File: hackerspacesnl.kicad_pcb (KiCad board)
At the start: 2 copper layers, 82.7 x 99.6 mm, 38 parts, among them J1 Screw_Terminal_01x02, J2 Conn_01x04_Male, Q1 Q_NMOS_GSD, Q2 Q_NMOS_GSD, Q3 Q_NMOS_GSD, Q4 Q_NMOS_GSD, Q5 Q_NMOS_GSD, Q6 Q_NMOS_GSD, SW1 SW_Push, SW2 SW_Push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

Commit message: led footprint
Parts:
- added D1: Red-GreenLED, hsnl:LED_0805_multicolor, F.Cu at (66.6, 90.7)
- added D10: Red-GreenLED, hsnl:LED_0805_multicolor, F.Cu at (80.0, 90.7)
- added D11: Red-GreenLED, hsnl:LED_0805_multicolor, F.Cu at (71.1, 99.9)
- added D12: Red-GreenLED, hsnl:LED_0805_multicolor, F.Cu at (75.5, 96.8)
- added D13: Red-GreenLED, hsnl:LED_0805_multicolor, F.Cu at (80.0, 93.8)
- added D14: Red-GreenLED, hsnl:LED_0805_multicolor, F.Cu at (84.4, 90.7)
- added D15: Red-GreenLED, hsnl:LED_0805_multicolor, F.Cu at (75.5, 99.9)
- added D2: Red-GreenLED, hsnl:LED_0805_multicolor, F.Cu at (66.6, 93.8)
- added D3: Red-GreenLED, hsnl:LED_0805_multicolor, F.Cu at (71.1, 90.7)
- added D4: Red-GreenLED, hsnl:LED_0805_multicolor, F.Cu at (66.6, 96.8)
- added D5: Red-GreenLED, hsnl:LED_0805_multicolor, F.Cu at (71.1, 93.8)
- added D6: Red-GreenLED, hsnl:LED_0805_multicolor, F.Cu at (75.5, 90.7)
- added D7: Red-GreenLED, hsnl:LED_0805_multicolor, F.Cu at (66.6, 99.9)
- added D8: Red-GreenLED, hsnl:LED_0805_multicolor, F.Cu at (71.1, 96.8)
- added D9: Red-GreenLED, hsnl:LED_0805_multicolor, F.Cu at (75.5, 93.8)

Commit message: board outline
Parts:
- moved D5 43.9 mm to (100.5, 126.4)
- moved D9 43.9 mm to (104.9, 126.4)
- moved D12 43.9 mm to (104.9, 129.5)
- moved D3 43.9 mm to (100.5, 123.4)
- moved D6 43.9 mm to (104.9, 123.4)
- moved D8 43.9 mm to (100.5, 129.5)
- moved D13 43.9 mm to (109.4, 126.4)
- moved D2 43.9 mm to (96.0, 126.4)
- moved D1 43.9 mm to (96.0, 123.4)
- moved D10 43.9 mm to (109.4, 123.4)
- moved D11 43.9 mm to (100.5, 132.5)
- moved D14 43.9 mm to (113.8, 123.4)
- moved D15 43.9 mm to (104.9, 132.5)
- moved D4 43.9 mm to (96.0, 129.5)
- moved D7 43.9 mm to (96.0, 132.5)
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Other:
- board size 82.7 x 99.6 mm -> 79.5 x 95.2 mm

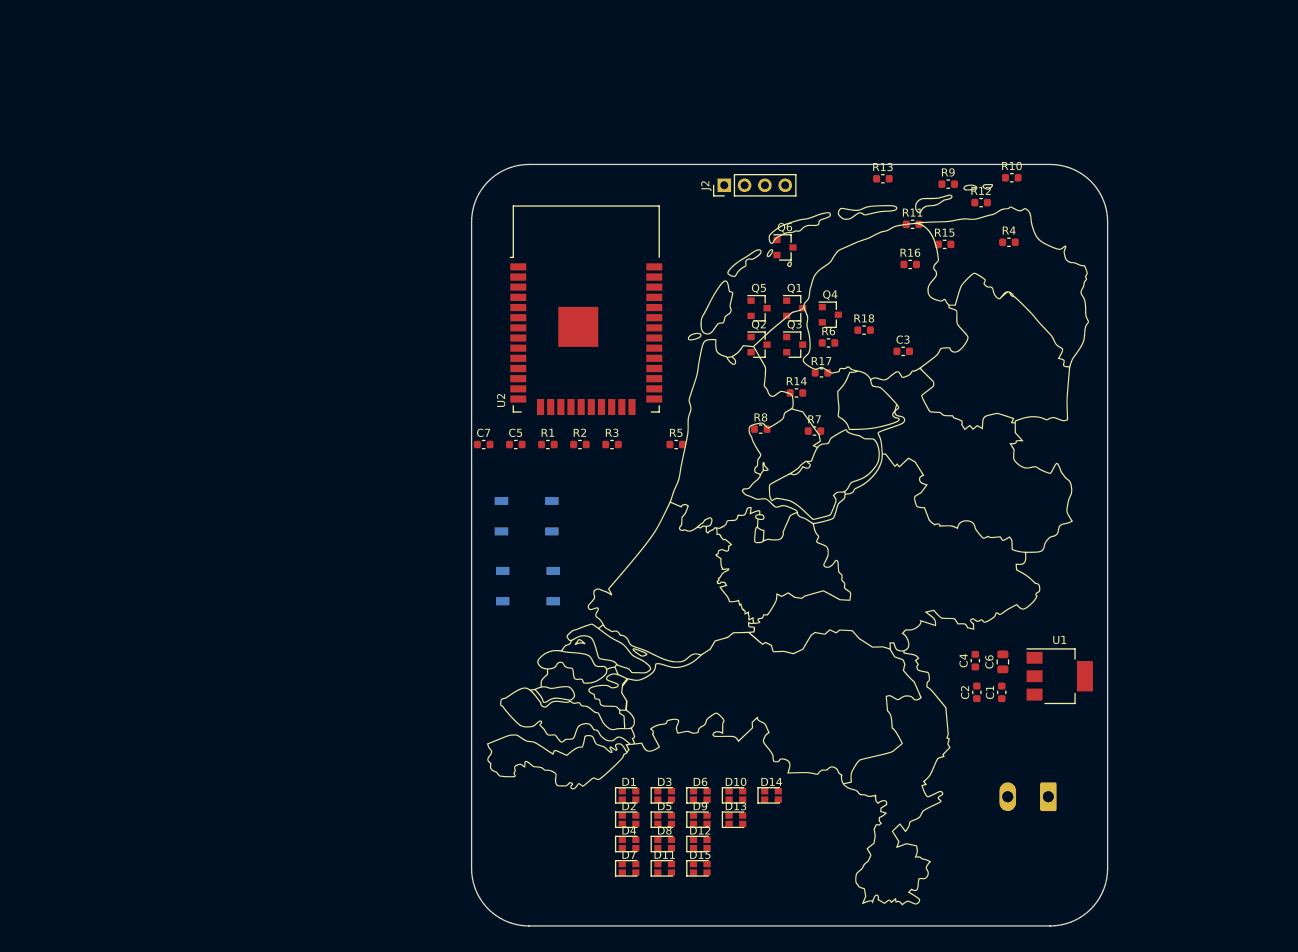
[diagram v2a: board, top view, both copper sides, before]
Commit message: fixed LED symbol, began initial layout
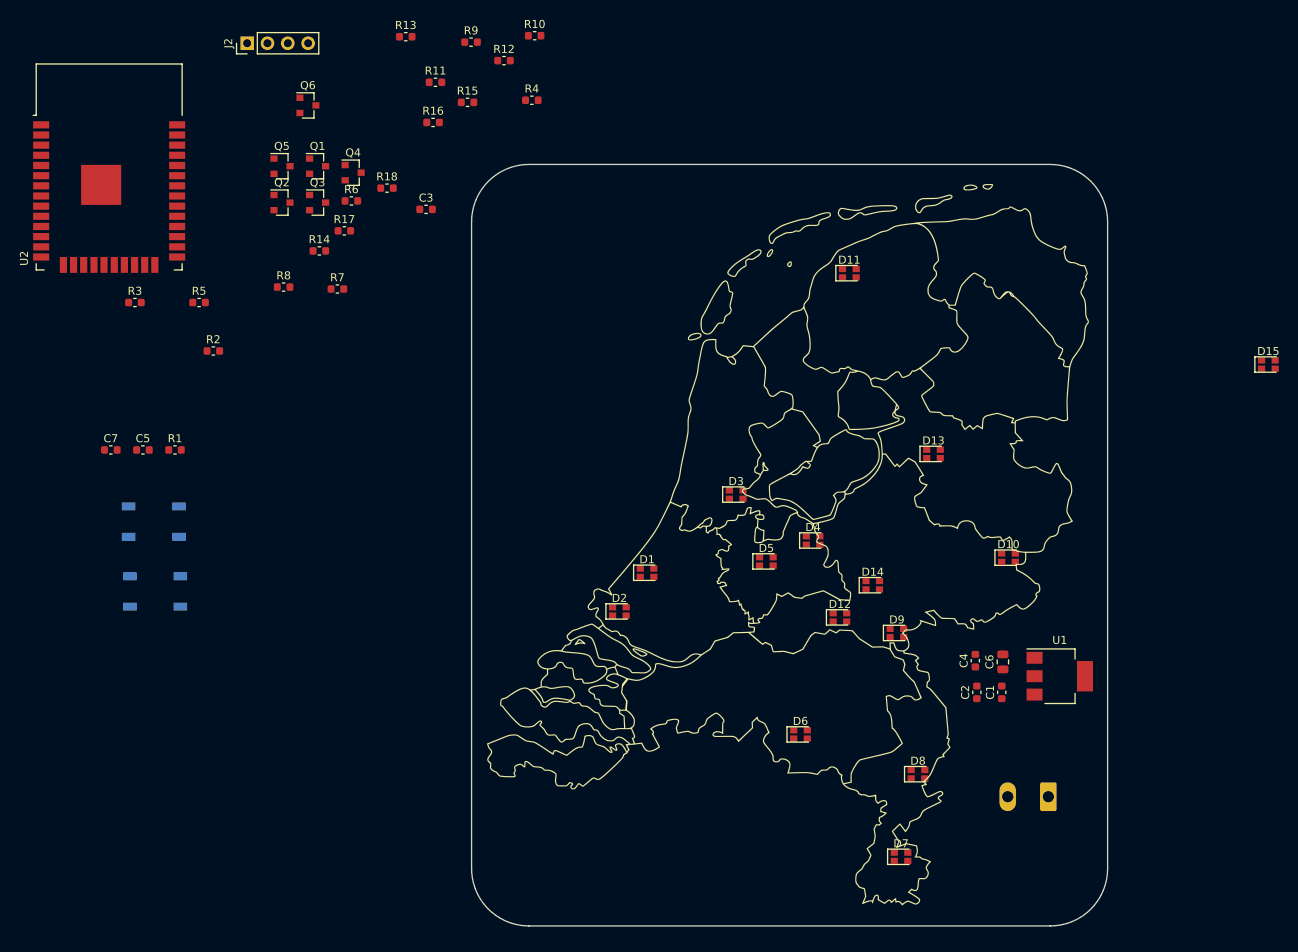
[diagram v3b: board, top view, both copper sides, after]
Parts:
- D4: value Red-GreenLED -> Red-GreenLED-parts
- moved D15 94.9 mm to (175.9, 69.5)
- moved D11 77.9 mm to (123.5, 58.1)
- moved R11 62.2 mm to (71.8, 34.2)
- moved Q4 62.2 mm to (61.5, 45.5)
- moved R7 62.2 mm to (59.6, 60.1)
- moved R8 62.2 mm to (52.8, 59.8)
- moved C3 62.2 mm to (70.6, 50.1)
- moved J2 62.2 mm to (48.3, 29.4)
- moved Q1 62.2 mm to (57.1, 44.7)
- moved Q2 62.2 mm to (52.6, 49.3)
- moved Q3 62.2 mm to (57.1, 49.3)
- moved Q5 62.2 mm to (52.6, 44.7)
- moved Q6 62.2 mm to (55.9, 37.1)
- moved R10 62.2 mm to (84.2, 28.4)
- moved R12 62.2 mm to (80.4, 31.5)
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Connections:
- D1 pad 1: (no net) -> Net-(D1-Pad1)
- D1 pad 2: (no net) -> Net-(D1-Pad2)
- D1 pad 3: (no net) -> Net-(D1-Pad3)
- D1 pad 4: (no net) -> Net-(D1-Pad4)
- D10 pad 1: (no net) -> Net-(D10-Pad1)
- D10 pad 2: (no net) -> Net-(D10-Pad2)
- D10 pad 3: (no net) -> Net-(D10-Pad3)
- D10 pad 4: (no net) -> Net-(D10-Pad4)
- D11 pad 1: (no net) -> Net-(D11-Pad1)
- D11 pad 2: (no net) -> Net-(D11-Pad2)
- D11 pad 3: (no net) -> Net-(D1-Pad3)
- D11 pad 4: (no net) -> Net-(D1-Pad4)
- D12 pad 1: (no net) -> Net-(D11-Pad1)
- D12 pad 2: (no net) -> Net-(D11-Pad2)
- D12 pad 3: (no net) -> Net-(D12-Pad3)
- D12 pad 4: (no net) -> Net-(D12-Pad4)
- D13 pad 1: (no net) -> Net-(D11-Pad1)
- D13 pad 2: (no net) -> Net-(D11-Pad2)
- D13 pad 3: (no net) -> Net-(D13-Pad3)
- D13 pad 4: (no net) -> Net-(D13-Pad4)
- D14 pad 1: (no net) -> Net-(D11-Pad1)
- D14 pad 2: (no net) -> Net-(D11-Pad2)
- D14 pad 3: (no net) -> Net-(D14-Pad3)
- D14 pad 4: (no net) -> Net-(D14-Pad4)
- D15 pad 1: (no net) -> Net-(D11-Pad1)
- D15 pad 2: (no net) -> Net-(D11-Pad2)
- D15 pad 3: (no net) -> Net-(D10-Pad3)
- D15 pad 4: (no net) -> Net-(D10-Pad4)
- D2 pad 1: (no net) -> Net-(D1-Pad1)
- D2 pad 2: (no net) -> Net-(D1-Pad2)
- D2 pad 3: (no net) -> Net-(D12-Pad3)
- D2 pad 4: (no net) -> Net-(D12-Pad4)
- D3 pad 1: (no net) -> Net-(D1-Pad1)
- D3 pad 2: (no net) -> Net-(D1-Pad2)
- D3 pad 3: (no net) -> Net-(D13-Pad3)
- D3 pad 4: (no net) -> Net-(D13-Pad4)
- D4 pad 1: (no net) -> Net-(D1-Pad1)
- D4 pad 2: (no net) -> Net-(D1-Pad2)
- D4 pad 3: (no net) -> Net-(D14-Pad3)
- D4 pad 4: (no net) -> Net-(D14-Pad4)
- D5 pad 1: (no net) -> Net-(D1-Pad1)
- D5 pad 2: (no net) -> Net-(D1-Pad2)
- D5 pad 3: (no net) -> Net-(D10-Pad3)
- D5 pad 4: (no net) -> Net-(D10-Pad4)
- D6 pad 1: (no net) -> Net-(D10-Pad1)
- D6 pad 2: (no net) -> Net-(D10-Pad2)
- D6 pad 3: (no net) -> Net-(D1-Pad3)
- D6 pad 4: (no net) -> Net-(D1-Pad4)
- D7 pad 1: (no net) -> Net-(D10-Pad1)
- D7 pad 2: (no net) -> Net-(D10-Pad2)
- D7 pad 3: (no net) -> Net-(D12-Pad3)
- D7 pad 4: (no net) -> Net-(D12-Pad4)
- D8 pad 1: (no net) -> Net-(D10-Pad1)
- D8 pad 2: (no net) -> Net-(D10-Pad2)
- D8 pad 3: (no net) -> Net-(D13-Pad3)
- D8 pad 4: (no net) -> Net-(D13-Pad4)
- D9 pad 1: (no net) -> Net-(D10-Pad1)
- D9 pad 2: (no net) -> Net-(D10-Pad2)
- D9 pad 3: (no net) -> Net-(D14-Pad3)
- D9 pad 4: (no net) -> Net-(D14-Pad4)
- Q1 pad 3: Net-(D1-Pad~) -> Net-(D1-Pad1)
- Q2 pad 3: Net-(D1-Pad~) -> Net-(D1-Pad2)
- Q3 pad 3: Net-(D10-Pad~) -> Net-(D10-Pad1)
- Q4 pad 3: Net-(D10-Pad~) -> Net-(D10-Pad2)
- Q5 pad 3: Net-(D11-Pad~) -> Net-(D11-Pad1)
- Q6 pad 3: Net-(D11-Pad~) -> Net-(D11-Pad2)
- R1 pad 1: Net-(D1-Pad~) -> Net-(D1-Pad3)
- R10 pad 1: Net-(D10-Pad~) -> Net-(D10-Pad4)
- R2 pad 1: Net-(D1-Pad~) -> Net-(D1-Pad4)
- R3 pad 1: Net-(D12-Pad~) -> Net-(D12-Pad3)
- R4 pad 1: Net-(D12-Pad~) -> Net-(D12-Pad4)
- R5 pad 1: Net-(D13-Pad~) -> Net-(D13-Pad3)
- R6 pad 1: Net-(D13-Pad~) -> Net-(D13-Pad4)
- R7 pad 1: Net-(D14-Pad~) -> Net-(D14-Pad3)
- R8 pad 1: Net-(D14-Pad~) -> Net-(D14-Pad4)
- R9 pad 1: Net-(D10-Pad~) -> Net-(D10-Pad3)
